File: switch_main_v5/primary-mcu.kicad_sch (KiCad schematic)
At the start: 50 parts, among them Q801 DMP21D0UFB-7B, U801 FM25CL64B-DG, U802 STM32H573IIKxQ, Y801 XRCGB25M000F3A16R0, Y802 ECS-.327-7-12QS-TR

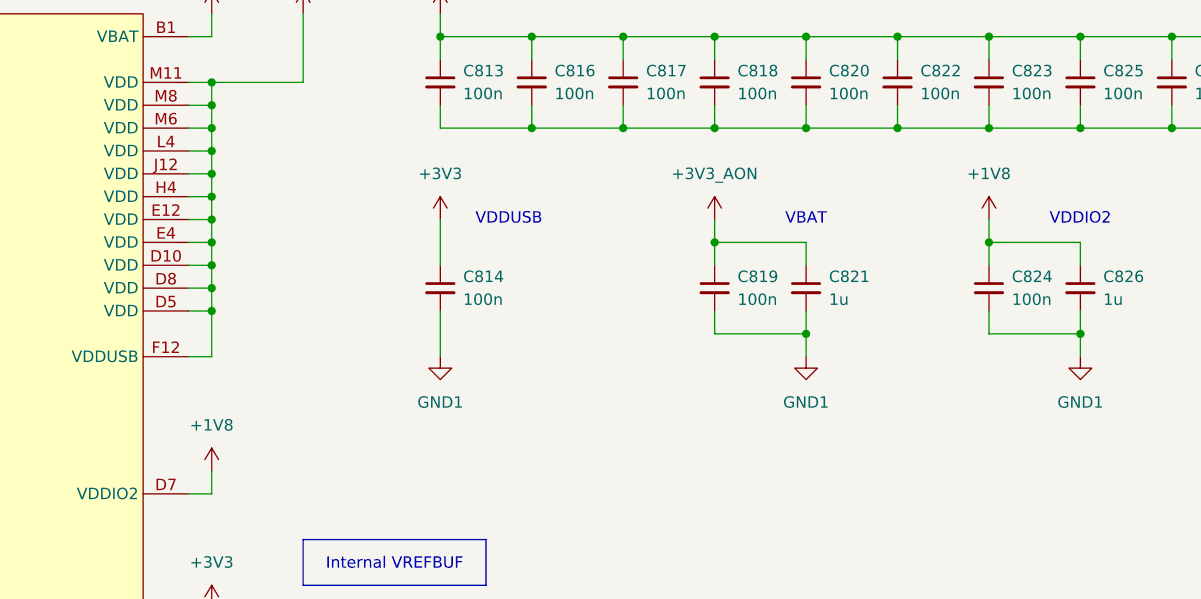
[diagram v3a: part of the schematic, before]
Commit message: Moved 0V9 regulators
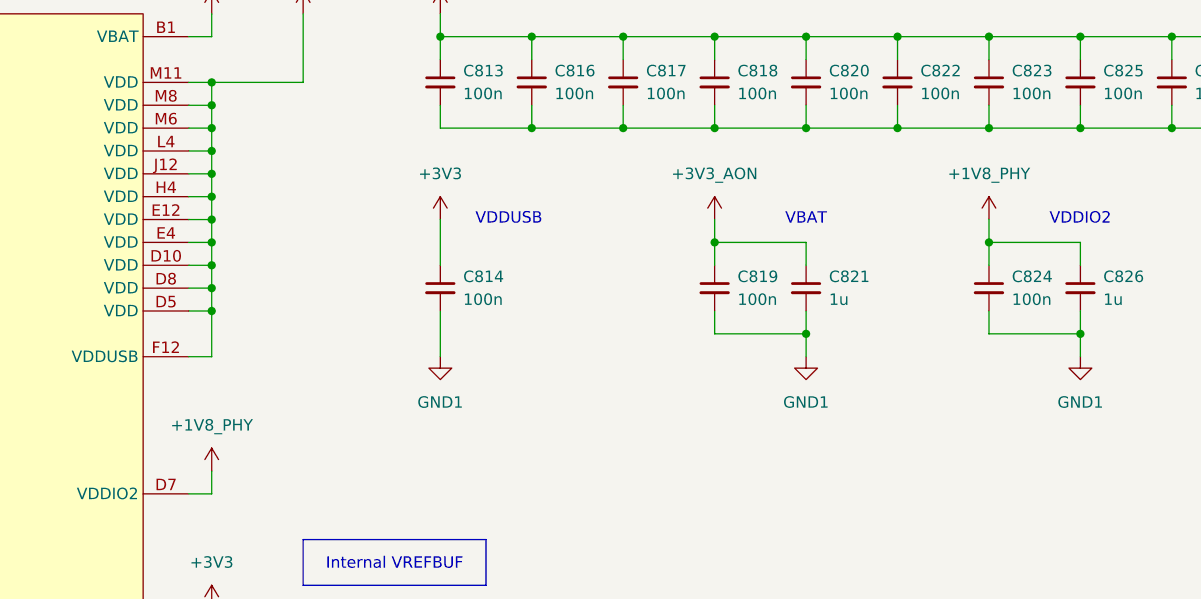
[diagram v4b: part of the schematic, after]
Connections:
- net +1V8 renamed +1V8_PHY
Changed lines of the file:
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@@
 	)
 	(symbol
-		(lib_id "power:+1V8")
-		(at 332.74 187.96 0)
-		(mirror y)
-		(unit 1)
-		(exclude_from_sim no)
-		(in_bom yes)
-		(on_board yes)
-		(dnp no)
-		(fields_autoplaced yes)
-		(property "Reference" "#PWR0824"
-			(at 332.74 191.77 0)
-			(effects
-				(font
-					(size 1.27 1.27)
-				)
-				(hide yes)
-			)
-		)
-		(property "Value" "+1V8"
-			(at 332.74 182.88 0)
-			(effects
-				(font
-					(size 1.27 1.27)
-				)
-			)
-		)
-		(property "Footprint" ""
-			(at 332.74 187.96 0)
-			(effects
-				(font
-					(size 1.27 1.27)
-				)
-				(hide yes)
-			)
-		)
-		(property "Datasheet" ""
-			(at 332.74 187.96 0)
-			(effects
-				(font
-					(size 1.27 1.27)
-				)
-				(hide yes)
-			)
-		)
-		(property "Description" "Power symbol creates a global label with name \"+1V8\""
-			(at 332.74 187.96 0)
-			(effects
-				(font
-					(size 1.27 1.27)
-				)
-				(hide yes)
-			)
-		)
-		(pin "1"
-		)
-		(instances
-			(project "switch_main_v4"
-				(path "/a5e57332-4284-4d3c-ab3c-13bc0ddb29b6/cc240678-80bc-4d6d-9d13-1541d9f89447"
-					(reference "#PWR0824")
-					(unit 1)
-				)
-			)
-		)
-	)
-	(symbol
 		(lib_id "Connector:TestPoint_Small")
 		(at 76.2 71.12 0)
@@
 	)
 	(symbol
-		(lib_id "power:+1V8")
-		(at 246.38 215.9 0)
-		(unit 1)
-		(exclude_from_sim no)
-		(in_bom yes)
-		(on_board yes)
-		(dnp no)
-		(fields_autoplaced yes)
-		(property "Reference" "#PWR0815"
-			(at 246.38 219.71 0)
-			(effects
-				(font
-					(size 1.27 1.27)
-				)
-				(hide yes)
-			)
-		)
-		(property "Value" "+1V8"
-			(at 246.38 210.82 0)
-			(effects
-				(font
-					(size 1.27 1.27)
-				)
-			)
-		)
-		(property "Footprint" ""
-			(at 246.38 215.9 0)
-			(effects
-				(font
-					(size 1.27 1.27)
-				)
-				(hide yes)
-			)
-		)
-		(property "Datasheet" ""
-			(at 246.38 215.9 0)
-			(effects
-				(font
-					(size 1.27 1.27)
-				)
-				(hide yes)
-			)
-		)
-		(property "Description" "Power symbol creates a global label with name \"+1V8\""
-			(at 246.38 215.9 0)
-			(effects
-				(font
-					(size 1.27 1.27)
-				)
-				(hide yes)
-			)
-		)
-		(pin "1"
-		)
-		(instances
-			(project ""
-				(path "/a5e57332-4284-4d3c-ab3c-13bc0ddb29b6/cc240678-80bc-4d6d-9d13-1541d9f89447"
-					(reference "#PWR0815")
-					(unit 1)
-				)
-			)
-		)
-	)
-	(symbol
 		(lib_id "power:+3V3")
 		(at 256.54 165.1 0)
@@
 	)
 	(symbol
+		(lib_id "PWR-SYM:+1V8_PHY")
+		(at 246.38 215.9 0)
+		(unit 1)
+		(exclude_from_sim no)
+		(in_bom yes)
+		(on_board yes)
+		(dnp no)
+		(fields_autoplaced yes)
+		(property "Reference" "#PWR0830"
+			(at 246.38 219.71 0)
+			(effects
+				(font
+					(size 1.27 1.27)
+				)
+				(hide yes)
+			)
+		)
+		(property "Value" "+1V8_PHY"
+			(at 246.38 210.82 0)
+			(effects
+				(font
+					(size 1.27 1.27)
+				)
+			)
+		)
+		(property "Footprint" ""
+			(at 246.38 215.9 0)
+			(effects
+				(font
+					(size 1.27 1.27)
+				)
+				(hide yes)
+			)
+		)
+		(property "Datasheet" ""
+			(at 246.38 215.9 0)
+			(effects
+				(font
+					(size 1.27 1.27)
+				)
+				(hide yes)
+			)
+		)
+		(property "Description" "Power symbol creates a global label with name \"+1V8_PHY\""
+			(at 246.38 215.9 0)
+			(effects
+				(font
+					(size 1.27 1.27)
+				)
+				(hide yes)
+			)
+		)
+		(pin "1"
+		)
+		(instances
+			(project "switch_main_v5"
+				(path "/a5e57332-4284-4d3c-ab3c-13bc0ddb29b6/cc240678-80bc-4d6d-9d13-1541d9f89447"
+					(reference "#PWR0830")
+					(unit 1)
+				)
+			)
+		)
+	)
+	(symbol
 		(lib_id "power:GND1")
 		(at 93.98 231.14 0)
@@
 					(unit 1)
 				)
+			)
+		)
+	)
+	(symbol
+		(lib_id "PWR-SYM:+1V8_PHY")
+		(at 332.74 187.96 0)
+		(mirror y)
+		(unit 1)
+		(exclude_from_sim no)
+		(in_bom yes)
+		(on_board yes)
+		(dnp no)
+		(fields_autoplaced yes)
+		(property "Reference" "#PWR0831"
+			(at 332.74 191.77 0)
+			(effects
+				(font
+					(size 1.27 1.27)
+				)
+				(hide yes)
+			)
+		)
+		(property "Value" "+1V8_PHY"
+			(at 332.74 182.88 0)
+			(effects
+				(font
+					(size 1.27 1.27)
+				)
+			)
+		)
+		(property "Footprint" ""
+			(at 332.74 187.96 0)
+			(effects
+				(font
+					(size 1.27 1.27)
+				)
+				(hide yes)
+			)
+		)
+		(property "Datasheet" ""
+			(at 332.74 187.96 0)
+			(effects
+				(font
+					(size 1.27 1.27)
+				)
+				(hide yes)
+			)
+		)
+		(property "Description" "Power symbol creates a global label with name \"+1V8_PHY\""
+			(at 332.74 187.96 0)
+			(effects
+				(font
+					(size 1.27 1.27)
+				)
+				(hide yes)
+			)
+		)
+		(pin "1"
+		)
+		(instances
+			(project "switch_main_v5"
+				(path "/a5e57332-4284-4d3c-ab3c-13bc0ddb29b6/cc240678-80bc-4d6d-9d13-1541d9f89447"
+					(reference "#PWR0831")
+					(unit 1)
+				)

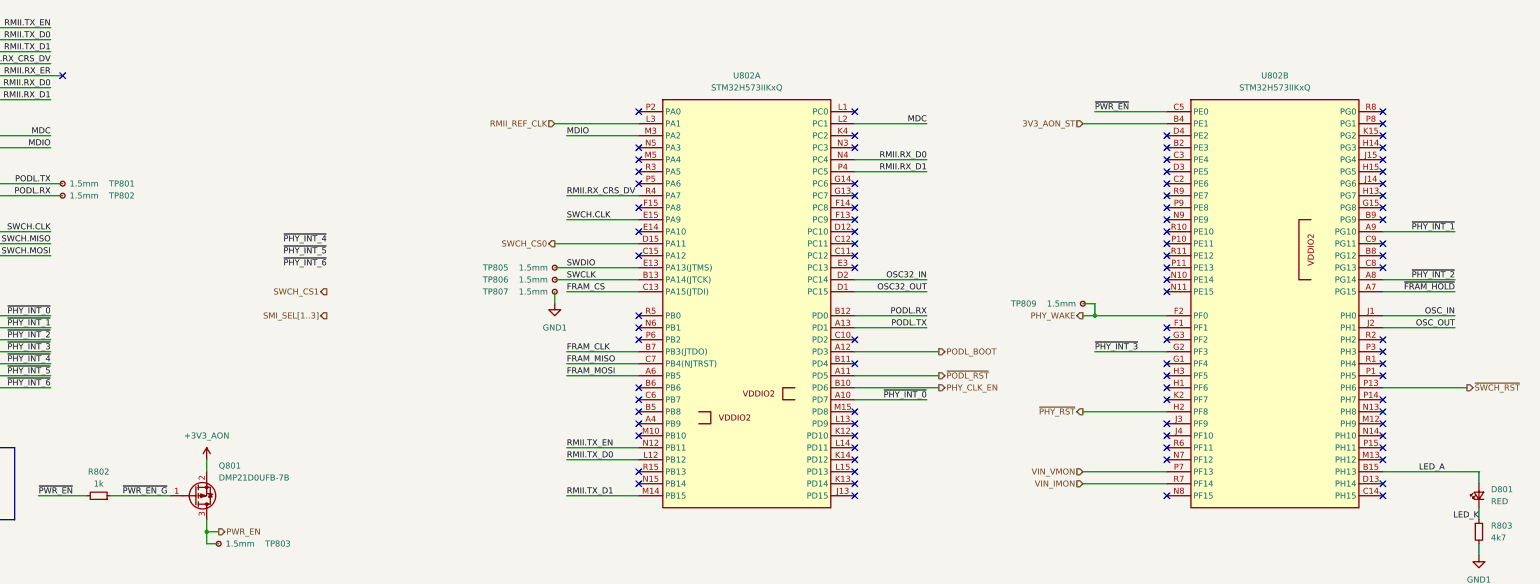
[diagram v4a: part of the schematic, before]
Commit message: All signals routed, need to do power still
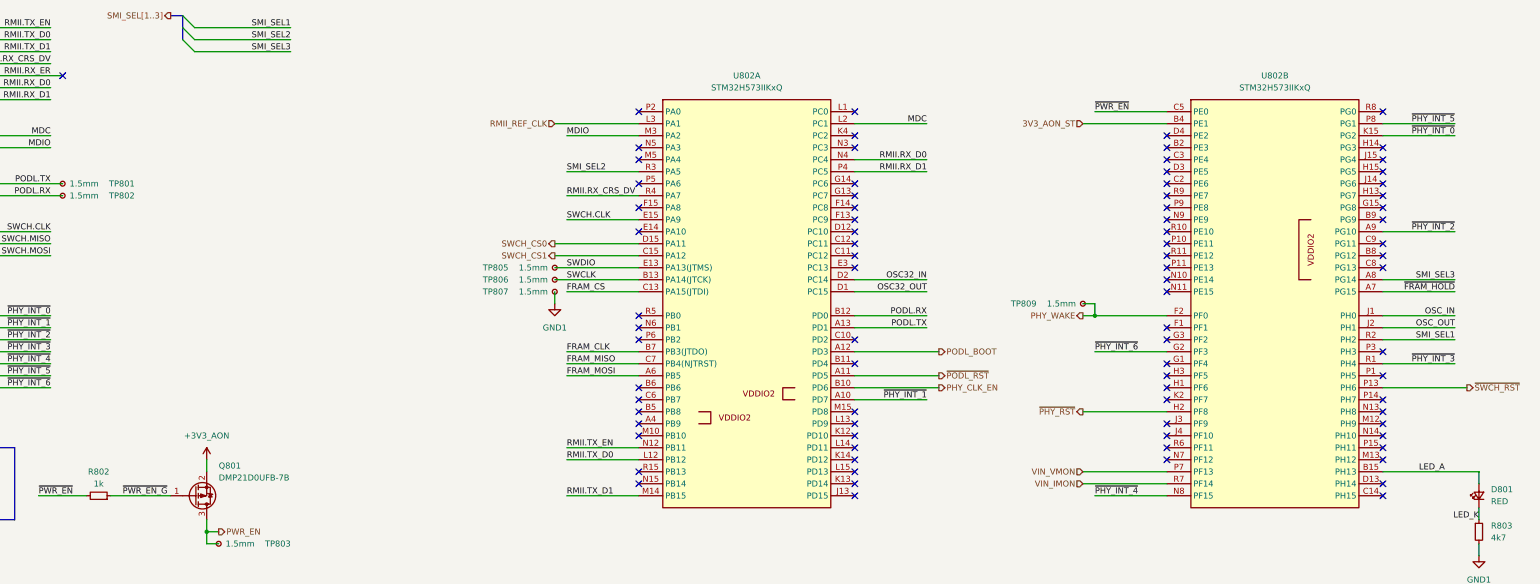
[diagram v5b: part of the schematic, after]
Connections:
- net SWCH_CS1: now also U802.C15 (PA12)
- net ~{PHY_INT_0}: now also U802.K15 (PG2); no longer U802.A10 (PD7)
- net ~{PHY_INT_1}: now also U802.A10 (PD7); no longer U802.A9 (PG10)
- net ~{PHY_INT_2}: now also U802.A9 (PG10); no longer U802.A8 (PG14)
- net ~{PHY_INT_3}: now also U802.R1 (PH4); no longer U802.G2 (PF3)
- net ~{PHY_INT_4}: now also U802.N8 (PF15)
- net ~{PHY_INT_5}: now also U802.P8 (PG1)
- net ~{PHY_INT_6}: now also U802.G2 (PF3)
- net SMI_SEL2: now reaches U802.R3 (PA5)
- net SMI_SEL1: now reaches U802.R2 (PH2)
- new net SMI_SEL3: U802.A8 (PG14)
- no-connect marks 98 -> 91

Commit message: Tidied schematic and PCB
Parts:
- renumbered C813 to C1401, C816 to C1402, C817 to C1403, C818 to C1404, C820 to C1405, C822 to C1406, C823 to C1407, C825 to C1408, C827 to C1409, C828 to C1410, C830 to C1411, C831 to C1412, C805 to C1413, C814 to C1414, C819 to C1415, C821 to C1416, C824 to C1417, C826 to C1418, C829 to C1419, C806 to C1420, C801 to C1421, C802 to C1422, C807 to C1423, C808 to C1424, C809 to C1425, C810 to C1426, C811 to C1427, C812 to C1428, C815 to C1429, C803 to C1430, C804 to C1431, D801 to D1401, L801 to L1401, Q801 to Q1401, R802 to R1401, R803 to R1402, R801 to R1403, TP801 to TP1401, TP802 to TP1402, TP805 to TP1403, TP806 to TP1404, TP807 to TP1405, TP809 to TP1406, TP803 to TP1407, TP804 to TP1408, TP808 to TP1409, U802 to U1401, U801 to U1402, Y801 to Y1401, Y802 to Y1402

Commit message: Updated crystal load capacitors
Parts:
- C1430, C1431: value 6p8 -> 22p
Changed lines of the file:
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@@
 			)
 		)
-		(property "Value" "6p8"
+		(property "Value" "22p"
 			(at 88.9064 252.73 90)
 			(effects
@@
 			)
 		)
-		(property "Value" "6p8"
+		(property "Value" "22p"
 			(at 88.9064 262.89 90)
 			(effects
